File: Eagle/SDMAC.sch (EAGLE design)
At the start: 3 parts, among them IC1 SUPER_DMAC_THT, J1 CORTEX_DEBUG_PTH, U1 XC95288XL-10TQG144C

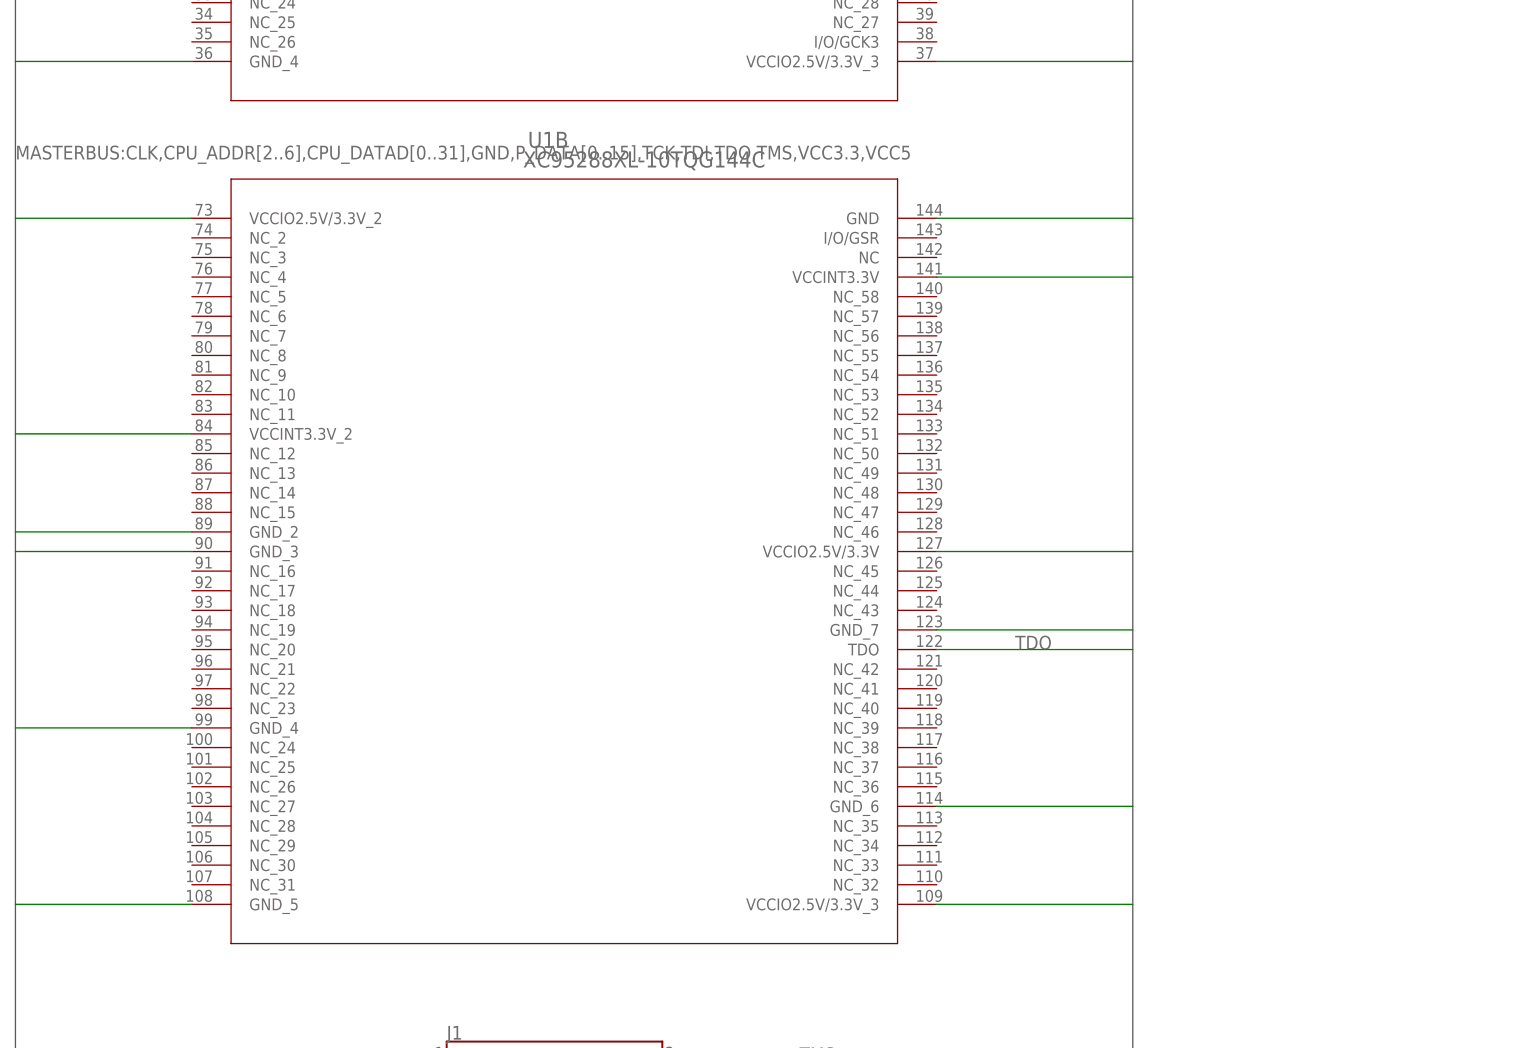
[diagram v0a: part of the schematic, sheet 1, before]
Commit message: added remaaining singnals to top and renamed them to be more consistant.
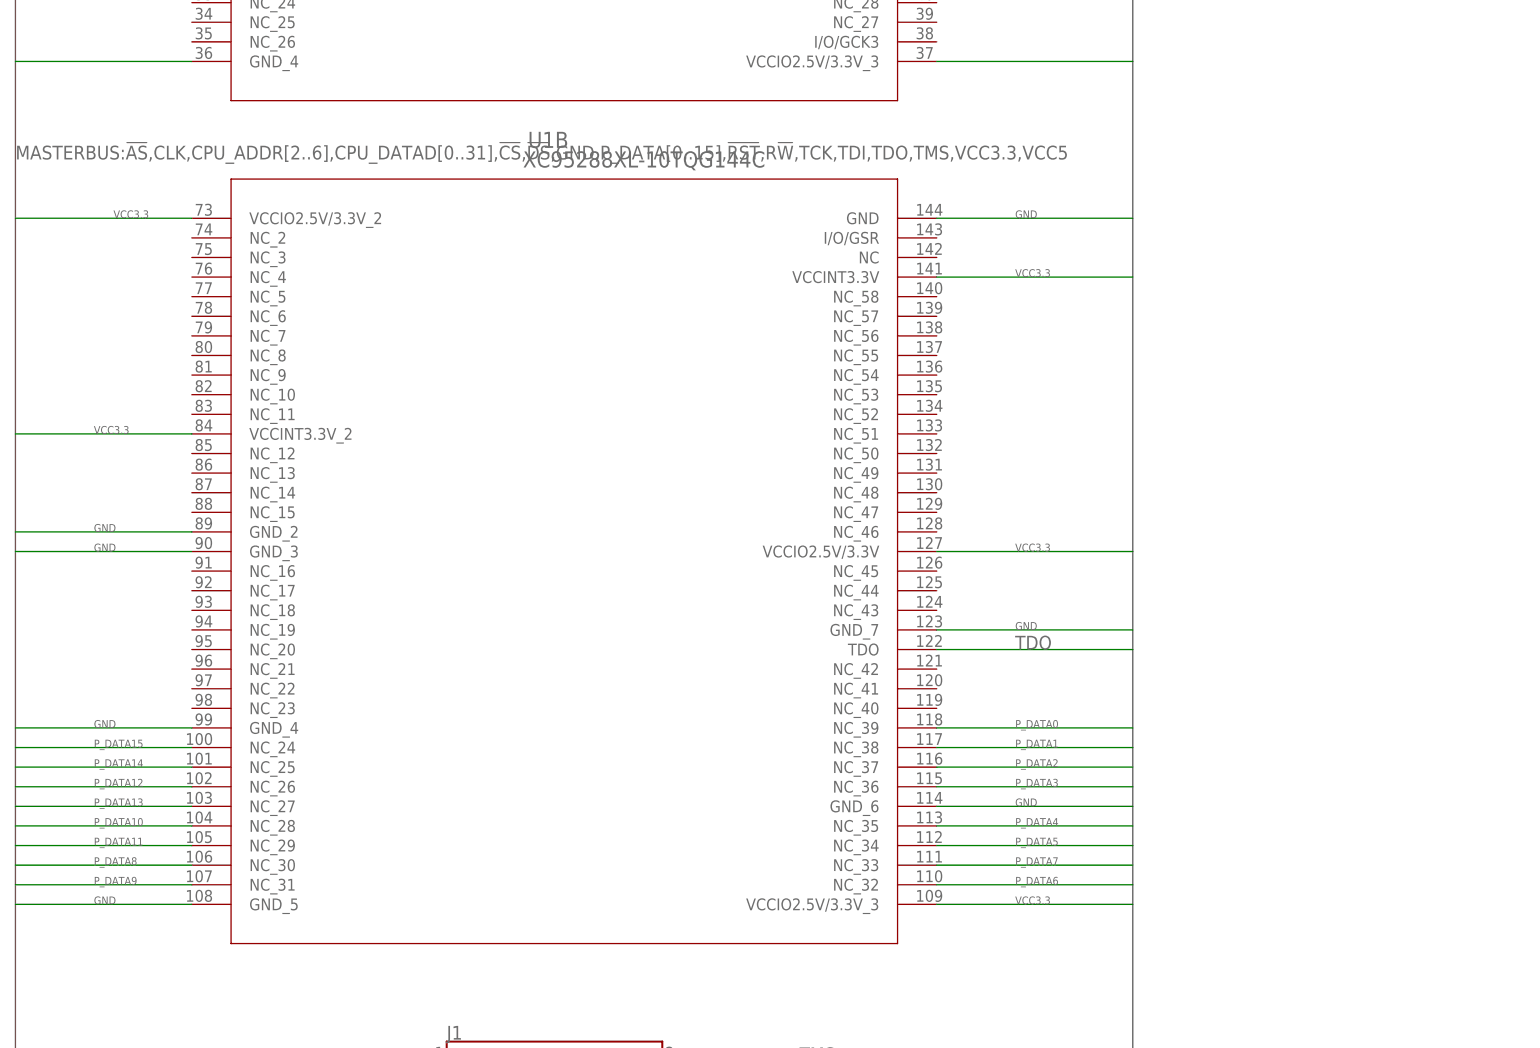
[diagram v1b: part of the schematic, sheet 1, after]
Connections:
- new net !AS: IC1.!AS
- new net !CS: IC1.!CS
- new net !DS: IC1.!DS
- new net !RST: IC1.!RESET
- new net R!W: IC1.R/!W!
- net P_DATA0: now also U1B.NC_39
- net P_DATA1: now also U1B.NC_38
- net P_DATA10: now also U1B.NC_28
- net P_DATA11: now also U1B.NC_29
- net P_DATA12: now also U1B.NC_26
- net P_DATA13: now also U1B.NC_27
- net P_DATA14: now also U1B.NC_25
- net P_DATA15: now also U1B.NC_24
- net P_DATA2: now also U1B.NC_37
- net P_DATA3: now also U1B.NC_36
- net P_DATA4: now also U1B.NC_35
- net P_DATA5: now also U1B.NC_34
- net P_DATA6: now also U1B.NC_32
- net P_DATA7: now also U1B.NC_33
- net P_DATA8: now also U1B.NC_30
- net P_DATA9: now also U1B.NC_31

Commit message: More updates
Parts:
- added C1, C2: 10uF, Capacitor:C_CHIP-0805(2012-METRIC)
- added U2: NCP1117ST33T3G, IC:NCP1117ST33T3G
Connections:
- net GND: now also C1.2, C2.2, U2.ADJ/GND
- net VCC3.3: now also C2.1, U2.4, U2.OUT
- net VCC5: now also C1.1, U2.IN

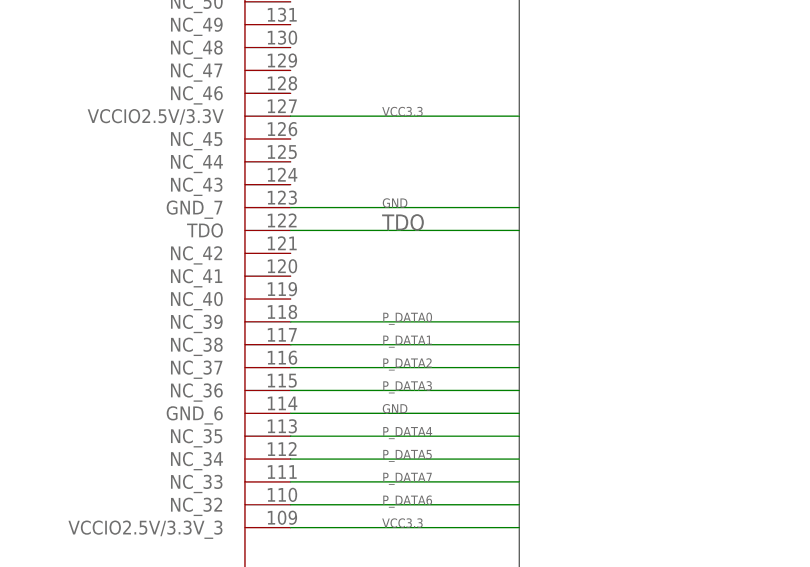
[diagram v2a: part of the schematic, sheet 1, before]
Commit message: setting pin assignments
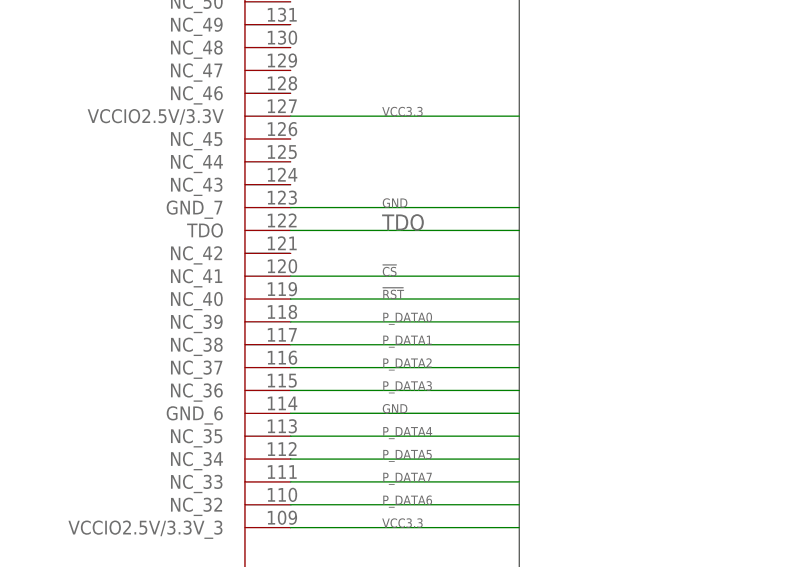
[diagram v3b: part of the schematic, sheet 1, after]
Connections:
- net !CS: now also U1B.NC_41
- net !RST: now also U1B.NC_40
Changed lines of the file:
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@@
 <grid distance="0.1" unitdist="inch" unit="inch" style="lines" multiple="1" display="no" altdistance="0.01" altunitdist="inch" altunit="inch"/>
 <layers>
-<layer number="1" name="Top" color="4" fill="1" visible="yes" active="no"/>
-<layer number="2" name="Route2" color="16" fill="1" visible="yes" active="no"/>
-<layer number="3" name="Route3" color="17" fill="1" visible="yes" active="no"/>
-<layer number="4" name="Route4" color="18" fill="1" visible="yes" active="no"/>
-<layer number="5" name="Route5" color="19" fill="1" visible="yes" active="no"/>
-<layer number="6" name="Route6" color="25" fill="1" visible="yes" active="no"/>
-<layer number="7" name="Route7" color="26" fill="1" visible="yes" active="no"/>
-<layer number="8" name="Route8" color="27" fill="1" visible="yes" active="no"/>
-<layer number="9" name="Route9" color="28" fill="1" visible="yes" active="no"/>
-<layer number="10" name="Route10" color="29" fill="1" visible="yes" active="no"/>
-<layer number="11" name="Route11" color="30" fill="1" visible="yes" active="no"/>
-<layer number="12" name="Route12" color="20" fill="1" visible="yes" active="no"/>
-<layer number="13" name="Route13" color="21" fill="1" visible="yes" active="no"/>
-<layer number="14" name="Route14" color="22" fill="1" visible="yes" active="no"/>
-<layer number="15" name="Route15" color="23" fill="1" visible="yes" active="no"/>
-<layer number="16" name="Bottom" color="1" fill="1" visible="yes" active="no"/>
-<layer number="17" name="Pads" color="2" fill="1" visible="yes" active="no"/>
-<layer number="18" name="Vias" color="2" fill="1" visible="yes" active="no"/>
-<layer number="19" name="Unrouted" color="6" fill="1" visible="yes" active="no"/>
-<layer number="20" name="Dimension" color="24" fill="1" visible="yes" active="no"/>
-<layer number="21" name="tPlace" color="7" fill="1" visible="yes" active="no"/>
-<layer number="22" name="bPlace" color="7" fill="1" visible="yes" active="no"/>
-<layer number="23" name="tOrigins" color="15" fill="1" visible="yes" active="no"/>
-<layer number="24" name="bOrigins" color="15" fill="1" visible="yes" active="no"/>
-<layer number="25" name="tNames" color="7" fill="1" visible="yes" active="no"/>
-<layer number="26" name="bNames" color="7" fill="1" visible="yes" active="no"/>
-<layer number="27" name="tValues" color="7" fill="1" visible="yes" active="no"/>
-<layer number="28" name="bValues" color="7" fill="1" visible="yes" active="no"/>
+<layer number="1" name="Top" color="4" fill="1" visible="no" active="no"/>
+<layer number="2" name="Route2" color="16" fill="1" visible="no" active="no"/>
+<layer number="3" name="Route3" color="17" fill="1" visible="no" active="no"/>
+<layer number="4" name="Route4" color="18" fill="1" visible="no" active="no"/>
+<layer number="5" name="Route5" color="19" fill="1" visible="no" active="no"/>
+<layer number="6" name="Route6" color="25" fill="1" visible="no" active="no"/>
+<layer number="7" name="Route7" color="26" fill="1" visible="no" active="no"/>
+<layer number="8" name="Route8" color="27" fill="1" visible="no" active="no"/>
+<layer number="9" name="Route9" color="28" fill="1" visible="no" active="no"/>
+<layer number="10" name="Route10" color="29" fill="1" visible="no" active="no"/>
+<layer number="11" name="Route11" color="30" fill="1" visible="no" active="no"/>
+<layer number="12" name="Route12" color="20" fill="1" visible="no" active="no"/>
+<layer number="13" name="Route13" color="21" fill="1" visible="no" active="no"/>
+<layer number="14" name="Route14" color="22" fill="1" visible="no" active="no"/>
+<layer number="15" name="Route15" color="23" fill="1" visible="no" active="no"/>
+<layer number="16" name="Bottom" color="1" fill="1" visible="no" active="no"/>
+<layer number="17" name="Pads" color="2" fill="1" visible="no" active="no"/>
+<layer number="18" name="Vias" color="2" fill="1" visible="no" active="no"/>
+<layer number="19" name="Unrouted" color="6" fill="1" visible="no" active="no"/>
+<layer number="20" name="Dimension" color="24" fill="1" visible="no" active="no"/>
+<layer number="21" name="tPlace" color="7" fill="1" visible="no" active="no"/>
+<layer number="22" name="bPlace" color="7" fill="1" visible="no" active="no"/>
+<layer number="23" name="tOrigins" color="15" fill="1" visible="no" active="no"/>
+<layer number="24" name="bOrigins" color="15" fill="1" visible="no" active="no"/>
+<layer number="25" name="tNames" color="7" fill="1" visible="no" active="no"/>
+<layer number="26" name="bNames" color="7" fill="1" visible="no" active="no"/>
+<layer number="27" name="tValues" color="7" fill="1" visible="no" active="no"/>
+<layer number="28" name="bValues" color="7" fill="1" visible="no" active="no"/>
 <layer number="29" name="tStop" color="7" fill="3" visible="no" active="no"/>
 <layer number="30" name="bStop" color="7" fill="6" visible="no" active="no"/>
@@
 <layer number="35" name="tGlue" color="7" fill="4" visible="no" active="no"/>
 <layer number="36" name="bGlue" color="7" fill="5" visible="no" active="no"/>
-<layer number="37" name="tTest" color="7" fill="1" visible="yes" active="no"/>
-<layer number="38" name="bTest" color="7" fill="1" visible="yes" active="no"/>
+<layer number="37" name="tTest" color="7" fill="1" visible="no" active="no"/>
+<layer number="38" name="bTest" color="7" fill="1" visible="no" active="no"/>
 <layer number="39" name="tKeepout" color="4" fill="11" visible="no" active="no"/>
 <layer number="40" name="bKeepout" color="1" fill="11" visible="no" active="no"/>
@@
 <layer number="44" name="Drills" color="7" fill="1" visible="no" active="no"/>
 <layer number="45" name="Holes" color="7" fill="1" visible="no" active="no"/>
-<layer number="46" name="Milling" color="3" fill="1" visible="yes" active="no"/>
-<layer number="47" name="Measures" color="7" fill="1" visible="yes" active="no"/>
-<layer number="48" name="Document" color="7" fill="1" visible="yes" active="no"/>
-<layer number="49" name="Reference" color="7" fill="1" visible="yes" active="no"/>
-<layer number="50" name="dxf" color="7" fill="1" visible="yes" active="no"/>
-<layer number="51" name="tDocu" color="7" fill="1" visible="yes" active="no"/>
-<layer number="52" name="bDocu" color="7" fill="1" visible="yes" active="no"/>
-<layer number="53" name="tGND_GNDA" color="7" fill="1" visible="yes" active="no"/>
-<layer number="54" name="bGND_GNDA" color="7" fill="1" visible="yes" active="no"/>
-<layer number="56" name="wert" color="7" fill="1" visible="yes" active="no"/>
-<layer number="57" name="tCAD" color="7" fill="1" visible="yes" active="no"/>
-<layer number="59" name="tCarbon" color="7" fill="1" visible="yes" active="no"/>
-<layer number="60" name="bCarbon" color="7" fill="1" visible="yes" active="no"/>
+<layer number="46" name="Milling" color="3" fill="1" visible="no" active="no"/>
+<layer number="47" name="Measures" color="7" fill="1" visible="no" active="no"/>
+<layer number="48" name="Document" color="7" fill="1" visible="no" active="no"/>
+<layer number="49" name="Reference" color="7" fill="1" visible="no" active="no"/>
+<layer number="50" name="dxf" color="7" fill="1" visible="no" active="no"/>
+<layer number="51" name="tDocu" color="7" fill="1" visible="no" active="no"/>
+<layer number="52" name="bDocu" color="7" fill="1" visible="no" active="no"/>
+<layer number="53" name="tGND_GNDA" color="7" fill="1" visible="no" active="no"/>
+<layer number="54" name="bGND_GNDA" color="7" fill="1" visible="no" active="no"/>
+<layer number="56" name="wert" color="7" fill="1" visible="no" active="no"/>
+<layer number="57" name="tCAD" color="7" fill="1" visible="no" active="no"/>
+<layer number="59" name="tCarbon" color="7" fill="1" visible="no" active="no"/>
+<layer number="60" name="bCarbon" color="7" fill="1" visible="no" active="no"/>
 <layer number="88" name="SimResults" color="9" fill="1" visible="yes" active="yes"/>
 <layer number="89" name="SimProbes" color="9" fill="1" visible="yes" active="yes"/>
@@
 </segment>
 </net>
+<net name="!RST" class="0">
+<segment>
+<pinref part="U1" gate="B" pin="NC_40"/>
+<wire x1="134.62" y1="-88.9" x2="160.02" y2="-88.9" width="0.1524" layer="91"/>
+<label x="144.78" y="-88.9" size="1.016" layer="95"/>
+</segment>
+</net>
+<net name="!CS" class="0">
+<segment>
+<pinref part="U1" gate="B" pin="NC_41"/>
+<wire x1="134.62" y1="-86.36" x2="160.02" y2="-86.36" width="0.1524" layer="91"/>
+<label x="144.78" y="-86.36" size="1.016" layer="95"/>
+</segment>
+</net>
